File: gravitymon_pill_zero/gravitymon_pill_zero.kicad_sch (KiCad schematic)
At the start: 17 parts, among them J1 Wireless Charge, J2 Wireless Charge, J3 Force Config, J4 Balance 1, J5 Balance 2, J6 Balance 3, SW2 SW_SPST, U1 TP-4056, U8 DS18B20

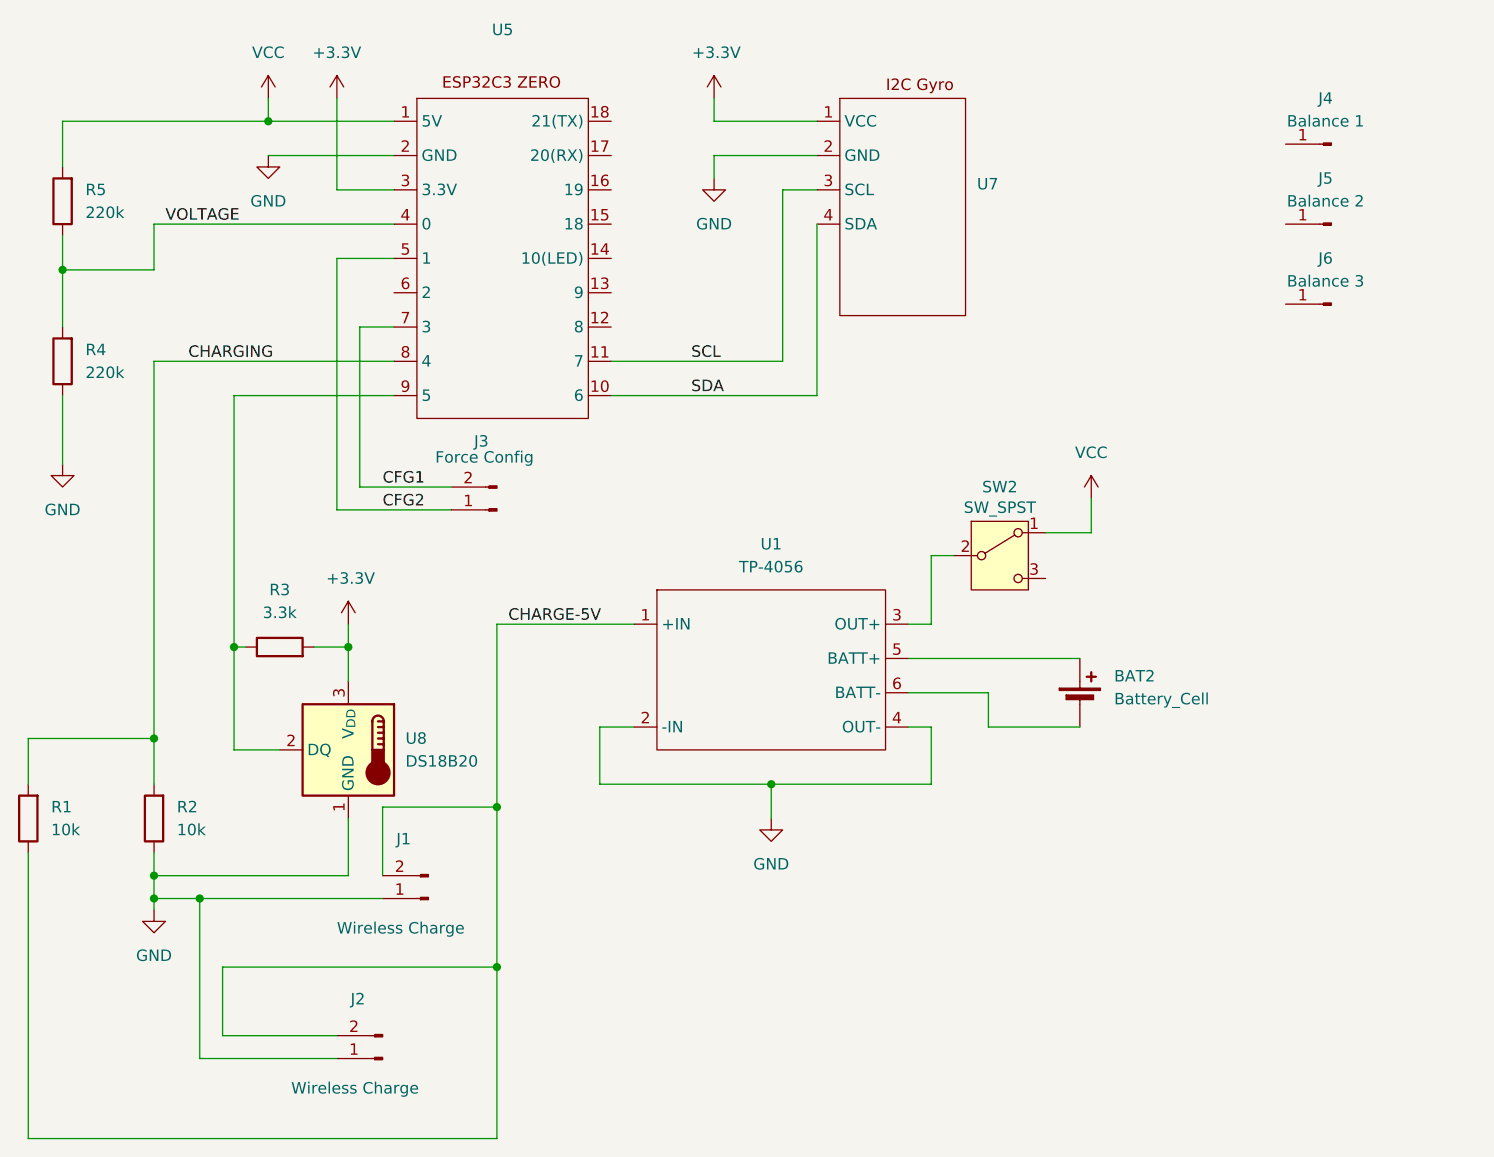
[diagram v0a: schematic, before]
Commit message: Update BOM for gravitymon
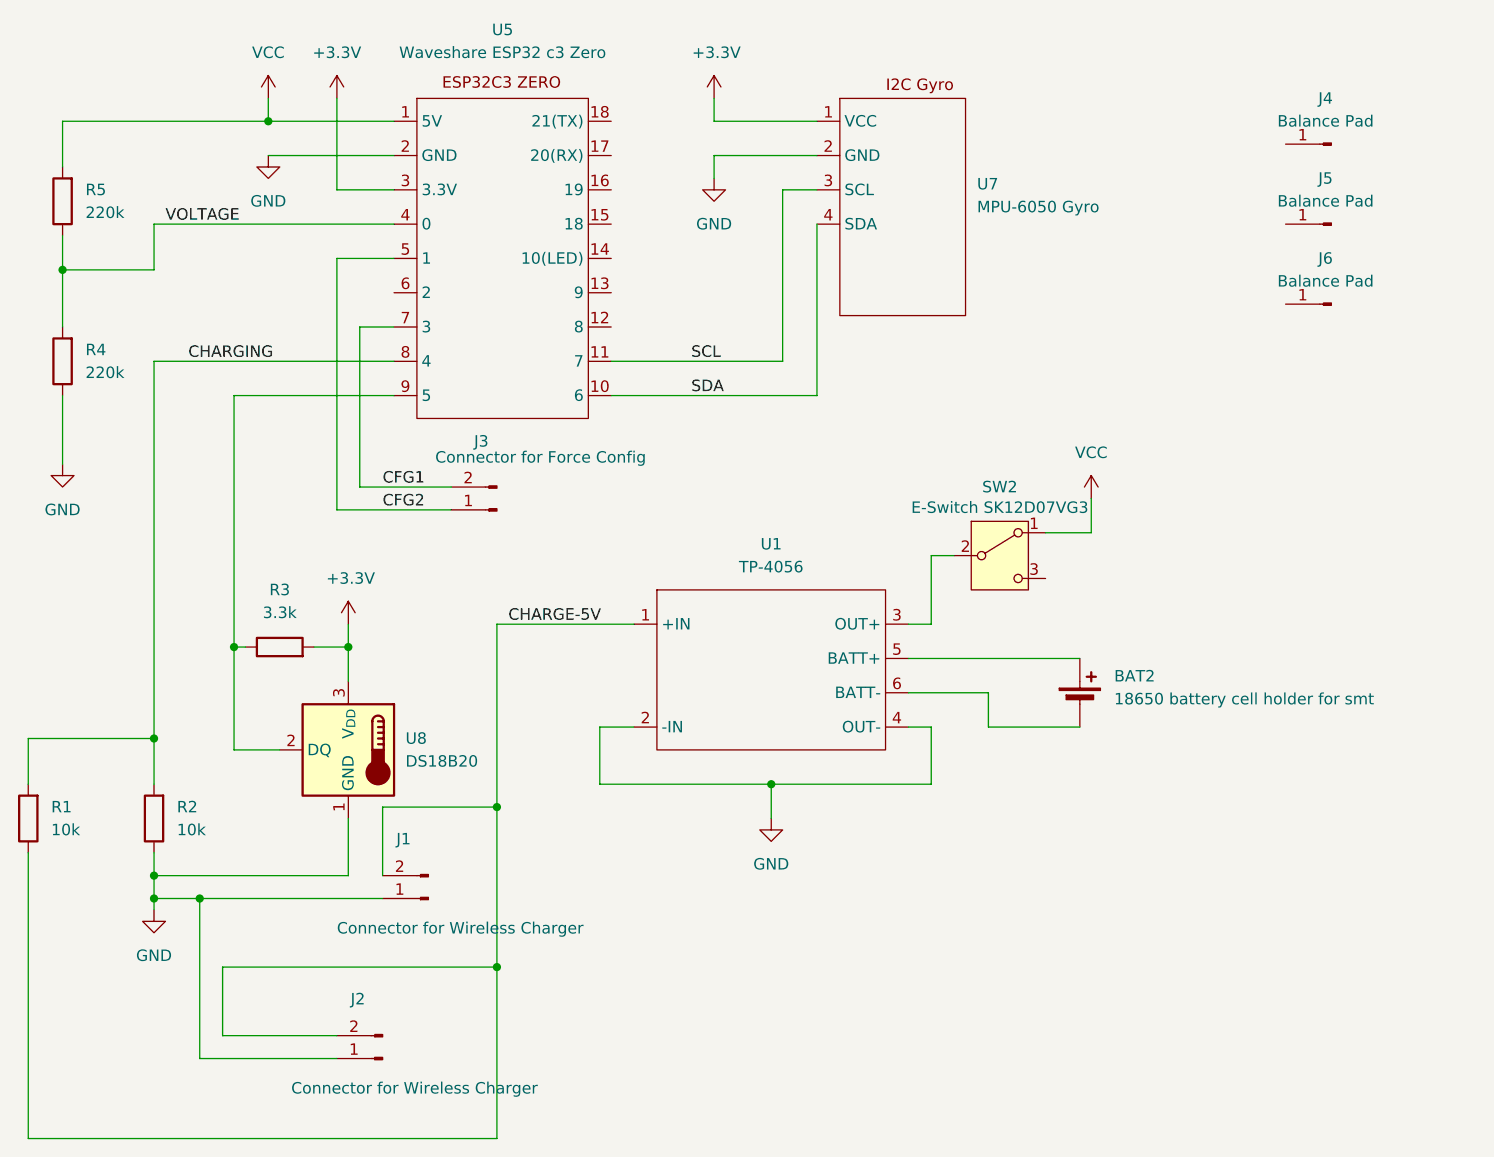
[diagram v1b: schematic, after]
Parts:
- BAT2: value Battery_Cell -> 18650 battery cell holder for smt
- J1, J2: value Wireless Charge -> Connector for Wireless Charger
- J3: value Force Config -> Connector for Force Config
- J4: value Balance 1 -> Balance Pad
- J5: value Balance 2 -> Balance Pad
- J6: value Balance 3 -> Balance Pad
- SW2: value SW_SPST -> E-Switch SK12D07VG3
- U5: value ~ -> Waveshare ESP32 c3 Zero
- U7: value ~ -> MPU-6050 Gyro
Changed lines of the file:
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@@
 			)
 		)
-		(property "Value" "Wireless Charge"
+		(property "Value" "Connector for Wireless Charger"
 			(at 105.41 149.352 0)
 			(effects
@@
 			)
 		)
-		(property "Value" "Balance 3"
+		(property "Value" "Balance Pad"
 			(at 220.345 59.69 0)
 			(effects
@@
 			)
 		)
-		(property "Value" "Balance 1"
+		(property "Value" "Balance Pad"
 			(at 220.345 41.91 0)
 			(effects
@@
 			)
 		)
-		(property "Description" ""
+		(property "Description" "TP-4056 LiPo charger with USB-C connector"
 			(at 147.32 97.79 0)
 			(effects
@@
 			)
 		)
-		(property "Value" "Battery_Cell"
+		(property "Value" "18650 battery cell holder for smt"
 			(at 196.85 106.1085 0)
 			(effects
@@
 			)
 		)
-		(property "Description" ""
+		(property "Description" "18650 battery cell holder for smt"
 			(at 193.04 106.68 0)
 			(effects
@@
 			)
 		)
-		(property "Description" ""
+		(property "Description" "DS18B20 one wire temperature sensor"
 			(at 111.76 111.76 0)
 			(effects
@@
 			)
 		)
-		(property "Value" "Force Config"
+		(property "Value" "Connector for Force Config"
 			(at 121.412 79.248 0)
 			(effects
@@
 			)
 		)
-		(property "Value" "~"
+		(property "Value" "Waveshare ESP32 c3 Zero"
 			(at 128.905 34.29 0)
 			(effects
@@
 			)
 		)
-		(property "Datasheet" ""
+		(property "Datasheet" "https://www.waveshare.com/wiki/ESP32-C3-Zero?srsltid=AfmBOopQp5_wdbmavH59V2WZeIh0hCY8uWPe9mviRX_U-7M7kkwxvOPk"
 			(at 123.19 59.69 0)
 			(effects
@@
 			)
 		)
-		(property "Description" ""
+		(property "Description" "Waveshare ESP32 c3 Zero"
 			(at 123.19 59.69 0)
 			(effects
@@
 			)
 		)
-		(property "Value" "SW_SPST"
+		(property "Value" "E-Switch SK12D07VG3"
 			(at 184.15 84.836 0)
 			(effects
@@
 			)
 		)
-		(property "Description" ""
+		(property "Description" "On / Off switch"
 			(at 184.15 90.17 0)
 			(effects
@@
 			)
 		)
-		(property "Value" "Wireless Charge"
+		(property "Value" "Connector for Wireless Charger"
 			(at 110.49 131.572 0)
 			(effects
@@
 			)
 		)
-		(property "Value" "Balance 2"
+		(property "Value" "Balance Pad"
 			(at 220.345 50.8 0)
 			(effects
@@
 			)
 		)
-		(property "Value" "~"
+		(property "Value" "MPU-6050 Gyro"
 			(at 181.61 51.4321 0)
 			(effects
@@
 			)
 		)
-		(property "Description" ""
+		(property "Description" "MPU-6050 Gyro"
 			(at 166.37 55.88 0)
 			(effects
